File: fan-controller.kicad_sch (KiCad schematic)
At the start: 17 parts, among them J8 Molex_KK_1x4_0470531000, U14 MAX31740ATA+T, U6 LP2985IM5X-5.0_SOT

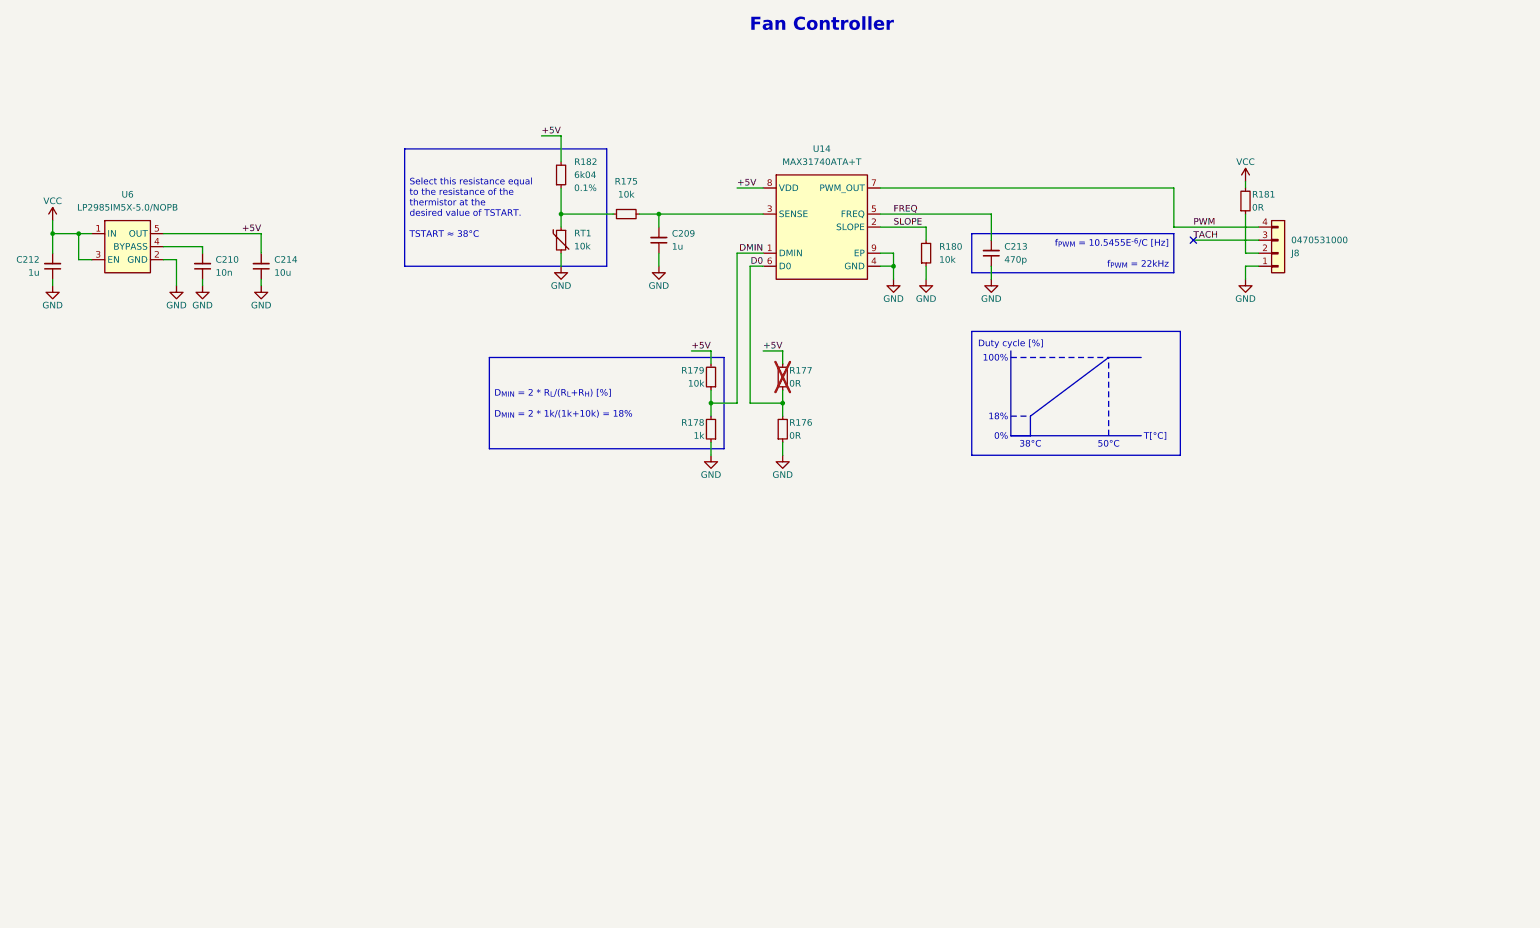
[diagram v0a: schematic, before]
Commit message: [#86851] Add option to set the fan supply to 5V, minor schematic readability improvement
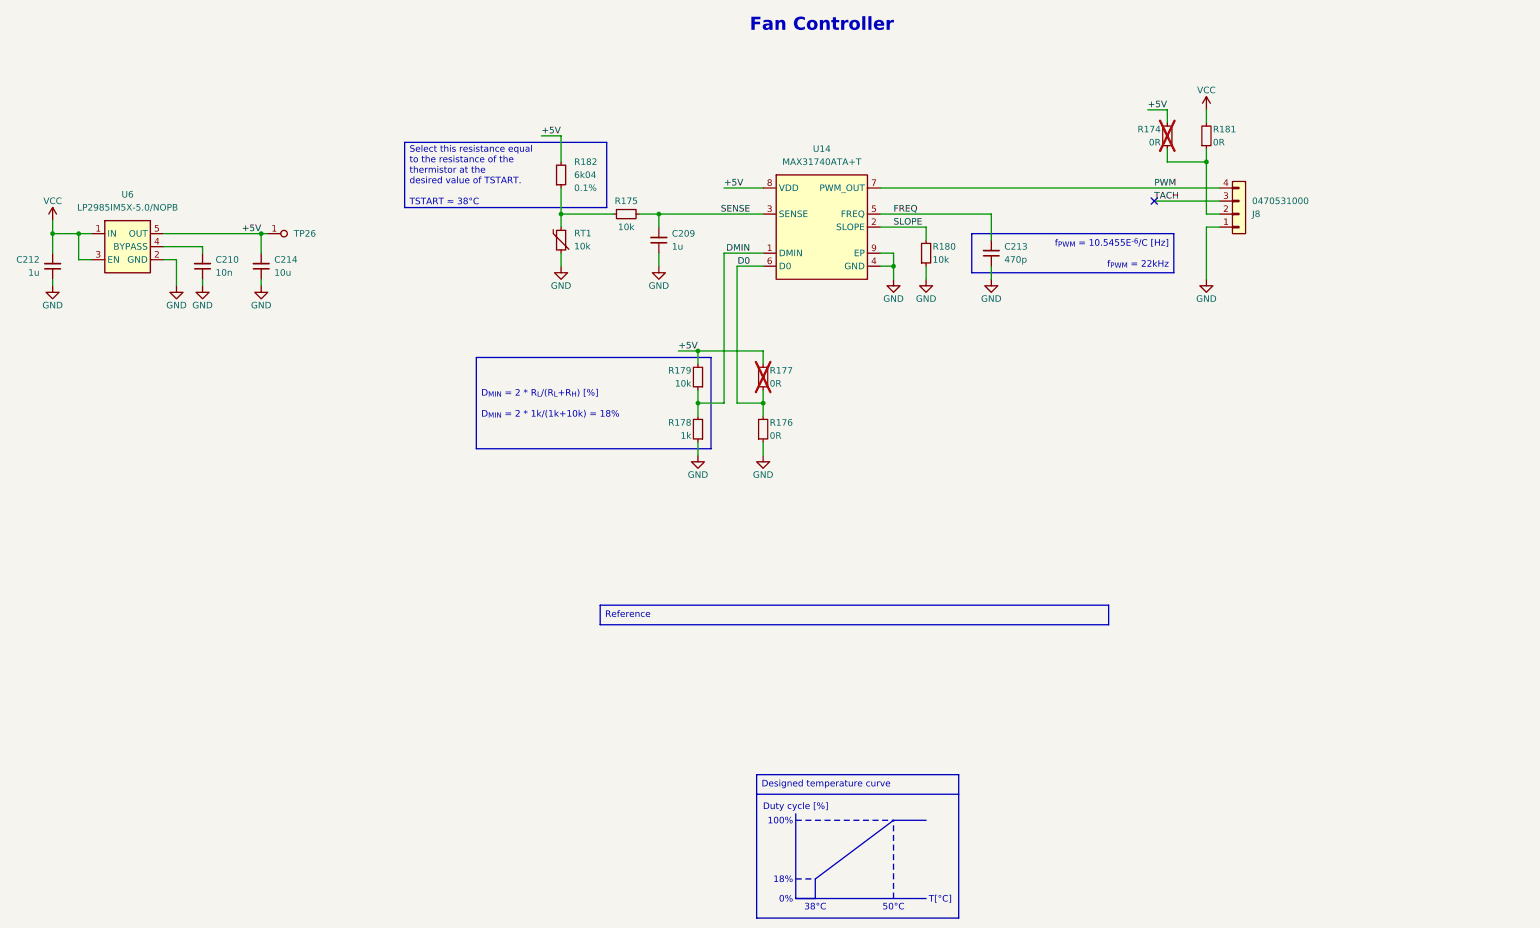
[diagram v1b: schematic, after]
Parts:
- added R174: R_0R_0402, antmicro-footprints:R_0402_1005Metric, symbol antmicroResistors0402:R_0R_0402
- added TP26: TP_0.75mm_SMD, antmicro-footprints:TP_SMD_0.75mm, symbol antmicroTestPoints:TP_0.75mm_SMD
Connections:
- net +5V: now also R174.2, TP26.1
- net at J8.2, R181.1: now also R174.1
- net SENSE: now reaches C209.2, R175.2, U14.3 (SENSE)
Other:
- moved on the sheet: J8, R176, R177, R178, R179, R181

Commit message: [#88407] Sch: Add PCIe ref clock; Add ICT testpoints; Add fan TVS
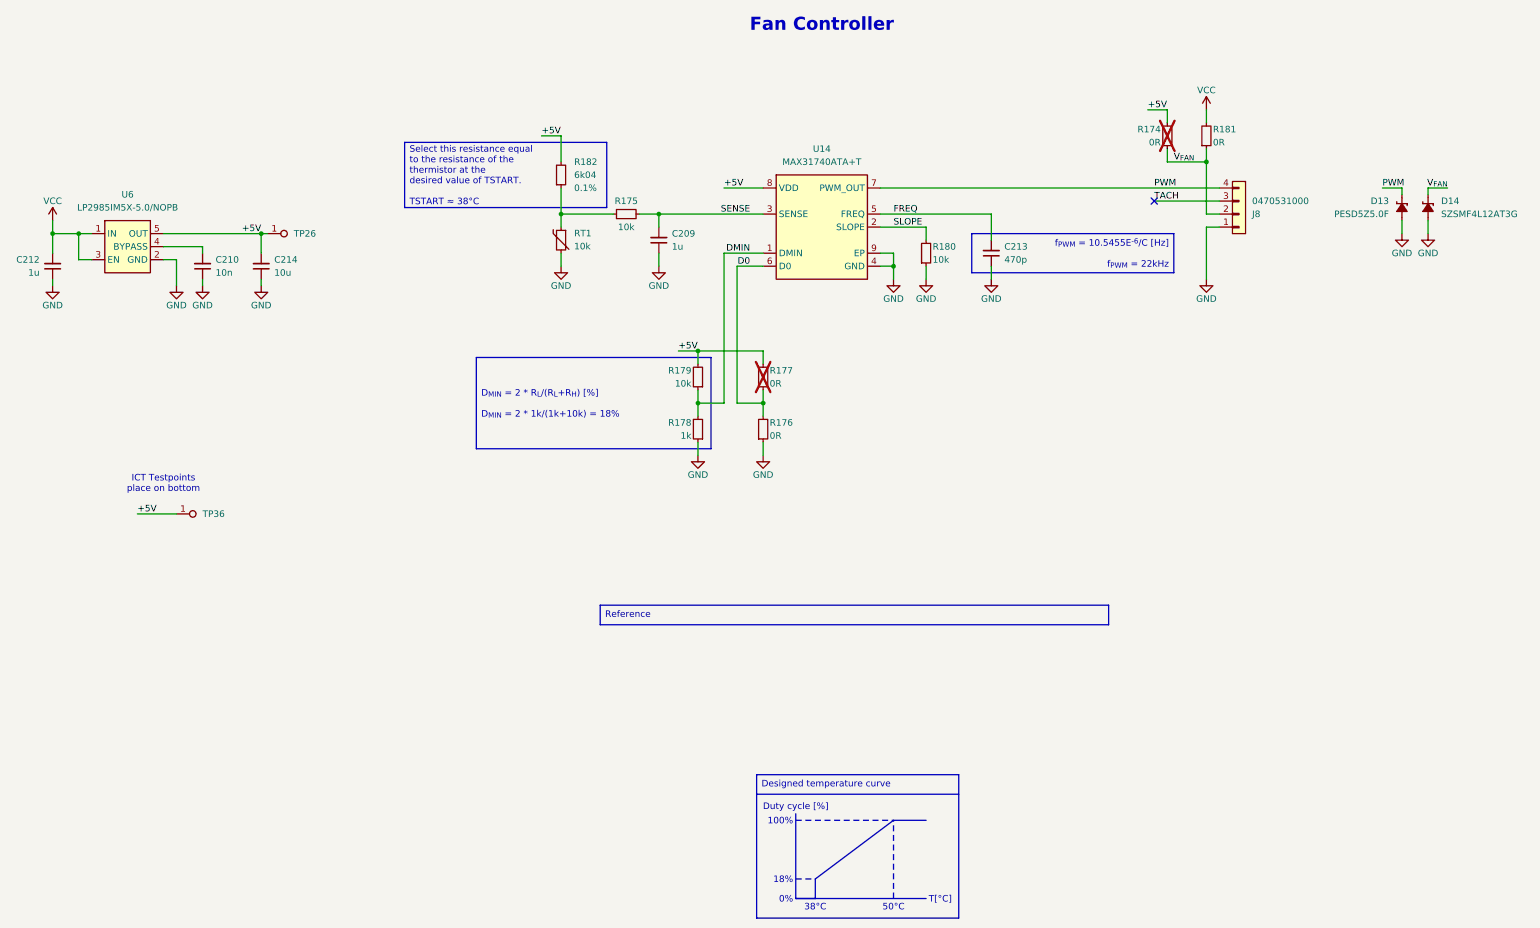
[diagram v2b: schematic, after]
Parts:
- added D13: PESD5Z5_0F, antmicro-footprints:SOD-523, symbol antmicroTVSDiodes:PESD5Z5_0F
- added D14: SZSMF4L14AT3G, antmicro-footprints:SOD-123FL, symbol antmicroTVSDiodes:SZSMF4L14AT3G
- added TP36: TP_1mm_SMD, antmicro-footprints:TP_SMD_1mm, symbol antmicroTestPoints:TP_1mm_SMD
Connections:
- net +5V: now also TP36.1
- net GND: now also D13.2 (A), D14.2 (A)
- net PWM: now also D13.1 (C)
- net V_{FAN}: now reaches J8.2, R174.1, R181.1
- net V_{FAN}: now also D14.1 (C)
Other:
- note added: "ICT Testpoints place on bottom"

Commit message: [#88407] Update date on SCH and PCB, fix 10k NTC footprint, change from 0603 to 0402
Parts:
- removed RT1: RT_NTC_10k_0603, antmicro-footprints:R_0603_1608Metric, symbol antmicroTemperatureSensorsAnalogandDigitalOutput:RT_NTC_10k_0603
- added RT1: RT_NTC_10k_0402, antmicro-footprints:R_0402_1005Metric, symbol antmicroTemperatureSensorsAnalogandDigitalOutput:RT_NTC_10k_0402
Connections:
- net GND: now also RT1.2
- net at R175.1, R182.1: now also RT1.1
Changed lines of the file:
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@@
 	(title_block
 		(title "OCuLink to 10GbE adapter")
-		(date "2025-12-23")
+		(date "2025-12-29")
 		(rev "1.0.0")
 		(company "Antmicro Ltd")
@@
 	)
 	(symbol
+		(lib_id "antmicroTemperatureSensorsAnalogandDigitalOutput:RT_NTC_10k_0402")
+		(at 153.67 139.7 270)
+		(unit 1)
+		(exclude_from_sim no)
+		(in_bom yes)
+		(on_board yes)
+		(dnp no)
+		(fields_autoplaced yes)
+		(property "Reference" "RT1"
+			(at 156.21 140.9065 90)
+			(effects
+				(font
+					(size 1.27 1.27)
+					(thickness 0.15)
+				)
+				(justify left)
+			)
+		)
+		(property "Value" "RT_NTC_10k_0402"
+			(at 143.51 160.02 0)
+			(effects
+				(font
+					(size 1.27 1.27)
+					(thickness 0.15)
+				)
+				(justify left bottom)
+				(hide yes)
+			)
+		)
+		(property "Footprint" "antmicro-footprints:R_0402_1005Metric"
+			(at 138.43 160.02 0)
+			(effects
+				(font
+					(size 1.27 1.27)
+					(thickness 0.15)
+				)
+				(justify left bottom)
+				(hide yes)
+			)
+		)
+		(property "Datasheet" "https://eu.mouser.com/datasheet/2/281/r44e-522712.pdf"
+			(at 135.89 160.02 0)
+			(effects
+				(font
+					(size 1.27 1.27)
+					(thickness 0.15)
+				)
+				(justify left bottom)
+				(hide yes)
+			)
+		)
+		(property "Description" "10k NTC in 0402 package with 5V max voltage"
+			(at 123.19 160.02 0)
+			(effects
+				(font
+					(size 1.27 1.27)
+				)
+				(justify left bottom)
+				(hide yes)
+			)
+		)
+		(property "MPN" "NCP15XH103F03RC"
+			(at 130.81 160.02 0)
+			(effects
+				(font
+					(size 1.27 1.27)
+				)
+				(justify left bottom)
+				(hide yes)
+			)
+		)
+		(property "Manufacturer" "Murata"
+			(at 133.35 160.02 0)
+			(effects
+				(font
+					(size 1.27 1.27)
+				)
+				(justify left bottom)
+				(hide yes)
+			)
+		)
+		(property "License" "Apache-2.0"
+			(at 125.73 160.02 0)
+			(effects
+				(font
+					(size 1.27 1.27)
+				)
+				(justify left bottom)
+				(hide yes)
+			)
+		)
+		(property "Author" "Antmicro"
+			(at 128.27 160.02 0)
+			(effects
+				(font
+					(size 1.27 1.27)
+				)
+				(justify left bottom)
+				(hide yes)
+			)
+		)
+		(property "Val" "10k"
+			(at 156.21 143.4464 90)
+			(effects
+				(font
+					(size 1.27 1.27)
+				)
+				(justify left)
+			)
+		)
+		(property "Voltage" "5V"
+			(at 140.97 160.02 0)
+			(effects
+				(font
+					(size 1.27 1.27)
+				)
+				(justify left bottom)
+				(hide yes)
+			)
+		)
+		(pin "1"
+		)
+		(pin "2"
+		)
+		(instances
+			(project ""
+				(path "/04bda987-e5eb-48b4-9e90-d8211dc11b39/cfdaa22c-cb6e-476e-82f5-94f72ae97682"
+					(reference "RT1")
+					(unit 1)
+				)
+			)
+		)
+	)
+	(symbol
 		(lib_id "antmicropower:GND")
 		(at 279.4 149.86 0)
@@
 					(unit 1)
 				)
-			)
-		)
-	)
-	(symbol
-		(lib_id "antmicroTemperatureSensorsAnalogandDigitalOutput:RT_NTC_10k_0603")
-		(at 153.67 139.7 270)
-		(unit 1)
-		(exclude_from_sim no)
-		(in_bom yes)
-		(on_board yes)
-		(dnp no)
-		(fields_autoplaced yes)
-		(property "Reference" "RT1"
-			(at 156.21 140.9065 90)
-			(effects
-				(font
-					(size 1.27 1.27)
-					(thickness 0.15)
-				)
-				(justify left)
-			)
-		)
-		(property "Value" "RT_NTC_10k_0603"
-			(at 143.51 160.02 0)
-			(effects
-				(font
-					(size 1.27 1.27)
-					(thickness 0.15)
-				)
-				(justify left bottom)
-				(hide yes)
-			)
-		)
-		(property "Footprint" "antmicro-footprints:R_0603_1608Metric"
-			(at 138.43 160.02 0)
-			(effects
-				(font
-					(size 1.27 1.27)
-					(thickness 0.15)
-				)
-				(justify left bottom)
-				(hide yes)
-			)
-		)
-		(property "Datasheet" "https://eu.mouser.com/datasheet/2/281/r44e-522712.pdf"
-			(at 135.89 160.02 0)
-			(effects
-				(font
-					(size 1.27 1.27)
-					(thickness 0.15)
-				)
-				(justify left bottom)
-				(hide yes)
-			)
-		)
-		(property "Description" "10k NTC in 0603 package with 5V max voltage"
-			(at 123.19 160.02 0)
-			(effects
-				(font
-					(size 1.27 1.27)
-				)
-				(justify left bottom)
-				(hide yes)
-			)
-		)
-		(property "MPN" "NCP15XH103F03RC"
-			(at 130.81 160.02 0)
-			(effects
-				(font
-					(size 1.27 1.27)
-				)
-				(justify left bottom)
-				(hide yes)
-			)
-		)
-		(property "Manufacturer" "Murata"
-			(at 133.35 160.02 0)
-			(effects
-				(font
-					(size 1.27 1.27)
-				)
-				(justify left bottom)
-				(hide yes)
-			)
-		)
-		(property "License" "Apache-2.0"
-			(at 125.73 160.02 0)
-			(effects
-				(font
-					(size 1.27 1.27)
-				)
-				(justify left bottom)
-				(hide yes)
-			)
-		)
-		(property "Author" "Antmicro"
-			(at 128.27 160.02 0)
-			(effects
-				(font
-					(size 1.27 1.27)
-				)
-				(justify left bottom)
-				(hide yes)
-			)
-		)
-		(property "Val" "10k"
-			(at 156.21 143.4464 90)
-			(effects
-				(font
-					(size 1.27 1.27)
-				)
-				(justify left)
-			)
-		)
-		(property "Voltage" "5V"
-			(at 140.97 160.02 0)
-			(effects
-				(font
-					(size 1.27 1.27)
-				)
-				(justify left bottom)
-				(hide yes)
-			)
-		)
-		(pin "1"
-		)
-		(pin "2"
-		)
-		(instances
-			(project "oculink-to-10gbe-adapter"
-				(path "/04bda987-e5eb-48b4-9e90-d8211dc11b39/cfdaa22c-cb6e-476e-82f5-94f72ae97682"
-					(reference "RT1")
-					(unit 1)
-				)
